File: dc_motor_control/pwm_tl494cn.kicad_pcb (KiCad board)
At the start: 2 copper layers, 70.6 x 45.5 mm, 46 parts, among them J1 PWR, J2 12V_SEL: up=src dn=reg, J3 MOT, Q1 RFP70N06, Q2 RFP70N06, Q3 RFP70N06, Q4 RFP70N06, Q5 BD139, Q6 BD140, U1 LM317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

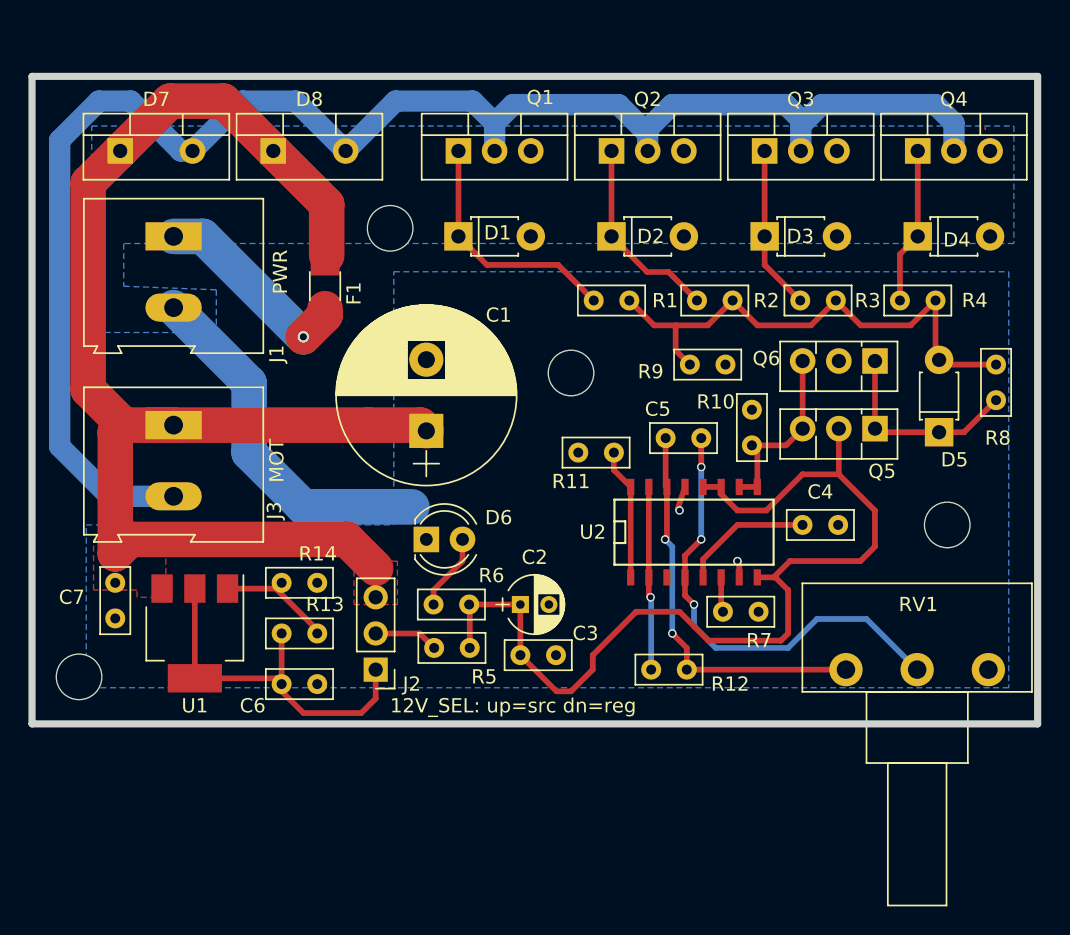
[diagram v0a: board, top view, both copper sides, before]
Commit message: Refining the DC motor control some more
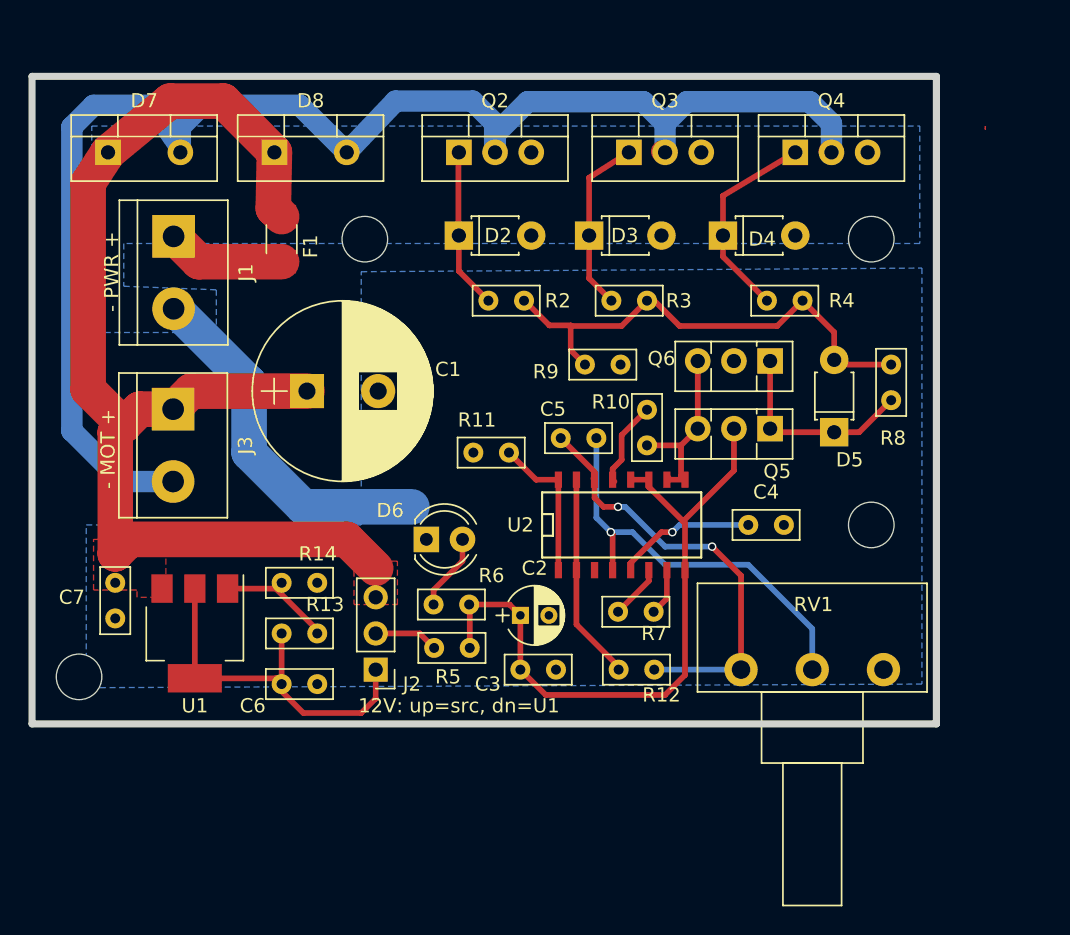
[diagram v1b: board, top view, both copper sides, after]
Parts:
- removed D1: 15V, Diodes_ThroughHole:D_T-1_P5.08mm_Horizontal
- removed Q1: RFP70N06, TO_SOT_Packages_THT:TO-220-3_Vertical
- removed R1: 10R, Capacitors_ThroughHole:C_Rect_L4.6mm_W2.0mm_P2.50mm_MKS02_FKP02
- J1: value PWR -> - PWR +; footprint Terminal_Blocks:TerminalBlock_Altech_AK300-2_P5.00mm -> Terminal_Blocks:TerminalBlock_bornier-2_P5.08mm
- J2: value 12V_SEL: up=src dn=reg -> 12V: up=src, dn=U1
- J3: value MOT -> - MOT +; footprint Terminal_Blocks:TerminalBlock_Altech_AK300-2_P5.00mm -> Terminal_Blocks:TerminalBlock_bornier-2_P5.08mm
- moved REF** 23.1 mm to (189.7, 91.7)
- moved R2 14.6 mm to (165.4, 96.0)
- moved D4 13.7 mm to (179.3, 91.4)
- moved R3 13.3 mm to (174.0, 96.0)
- moved D3 12.3 mm to (169.9, 91.4)
- moved Q2 10.7 mm to (160.8, 85.6)
- moved D2 10.7 mm to (160.8, 91.4)
- moved Q3 9.53 mm to (172.7, 85.6)
- moved R4 9.34 mm to (184.9, 96.0)
- moved C1 8.84 mm to (150.1, 102.4), turned to 0 degrees
- moved Q4 8.60 mm to (184.4, 85.6)
- moved C5 7.37 mm to (170.4, 105.7)
- moved D5 7.37 mm to (187.1, 105.2)
- moved Q5 7.37 mm to (182.6, 105.0)
- moved Q6 7.37 mm to (182.6, 100.2)
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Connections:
- U2 pad 3: Net-(U2-Pad3) -> (no net)
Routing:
- net +12V: track 68.4 -> 47.7 mm
- net Net-(D1-Pad1): track 17.4 -> 0.00 mm
- net Net-(C1-Pad1): track 95.8 -> 82.6 mm
- net Net-(D7-Pad2): track 112.9 -> 102.0 mm
- net GND: track 28.4 -> 34.8 mm, vias 2 -> 0
- net Net-(F1-Pad1): track 14.6 -> 8.32 mm, vias 1 -> 0
- net Net-(D4-Pad1): track 11.0 -> 14.6 mm
- net Net-(C5-Pad1): track 32.6 -> 29.6 mm, vias 3 -> 1
- net Net-(D2-Pad1): track 13.9 -> 11.4 mm
- net Net-(C5-Pad2): track 28.2 -> 30.5 mm
- net Net-(D5-Pad2): track 37.4 -> 35.2 mm
- net Net-(R12-Pad2): track 13.1 -> 14.8 mm, vias 1 -> 0
- net Net-(R7-Pad1): track 2.47 -> 3.99 mm
- net Net-(R11-Pad2): track 9.25 -> 10.6 mm
- net Net-(D3-Pad1): track 11.5 -> 12.7 mm
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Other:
- board size 70.6 x 45.5 mm -> 63.5 x 45.5 mm

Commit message: some more minor changes to the DC motor control PCB
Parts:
- moved R9 2.76 mm to (166.9, 100.6), turned to 180 degrees
- moved C5 1.02 mm to (170.4, 104.6)
- moved R10 1.02 mm to (174.0, 105.2)
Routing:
- net Net-(C5-Pad1): track 29.6 -> 30.6 mm
- net GND: track 34.8 -> 35.8 mm
- net Net-(C5-Pad2): track 30.5 -> 31.3 mm
- net Net-(Q5-Pad3): track 12.8 -> 13.3 mm
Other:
- board text added: "github.com/jonronen/kicad-stuff"
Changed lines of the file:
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@@
     (area 124.254857 80.013999 199.595143 139.195001)
     (thickness 1.6)
-    (drawings 4)
-    (tracks 172)
+    (drawings 5)
+    (tracks 175)
     (zones 0)
     (modules 43)
@@
     (last_trace_width 0.4)
     (trace_clearance 0.2)
-    (zone_clearance 1)
+    (zone_clearance 0.7)
     (zone_45_only no)
     (trace_min 0.2)
@@
   )
   (module Capacitors_ThroughHole:C_Rect_L4.6mm_W2.0mm_P2.50mm_MKS02_FKP02 (layer F.Cu)
-    (at 173.99 106.172 90)
+    (at 173.99 105.156 90)
     (descr "C, Rect series, Radial, pin pitch=2.50mm, , length*width=4.6*2mm^2, Capacitor, http://www.wima.de/DE/WIMA_MKS_02.pdf")
     (tags "C Rect series Radial pin pitch 2.50mm  length 4.6mm width 2mm Capacitor")
-    (fp_text reference R10 (at 3.048 -2.54 180) (layer F.SilkS)
+    (fp_text reference R10 (at 4.572 -2.54 180) (layer F.SilkS)
       (effects (font (size 1 1) (thickness 0.15)))
     )
@@
   )
   (module Capacitors_ThroughHole:C_Rect_L4.6mm_W2.0mm_P2.50mm_MKS02_FKP02 (layer F.Cu)
-    (at 170.434 105.664 180)
+    (at 170.434 104.648 180)
     (descr "C, Rect series, Radial, pin pitch=2.50mm, , length*width=4.6*2mm^2, Capacitor, http://www.wima.de/DE/WIMA_MKS_02.pdf")
     (tags "C Rect series Radial pin pitch 2.50mm  length 4.6mm width 2mm Capacitor")
-    (fp_text reference C5 (at 3.048 2.032 180) (layer F.SilkS)
+    (fp_text reference C5 (at 1.016 2.032 180) (layer F.SilkS)
       (effects (font (size 1 1) (thickness 0.15)))
     )
@@
   )
   (module Capacitors_ThroughHole:C_Rect_L4.6mm_W2.0mm_P2.50mm_MKS02_FKP02 (layer F.Cu)
-    (at 169.634 100.5)
+    (at 166.878 100.584 180)
     (descr "C, Rect series, Radial, pin pitch=2.50mm, , length*width=4.6*2mm^2, Capacitor, http://www.wima.de/DE/WIMA_MKS_02.pdf")
     (tags "C Rect series Radial pin pitch 2.50mm  length 4.6mm width 2mm Capacitor")
-    (fp_text reference R9 (at -2.75 0.5) (layer F.SilkS)
-      (effects (font (size 1 1) (thickness 0.15)))
-    )
-    (fp_text value 10K (at 1.25 2.31) (layer F.Fab) hide
+    (fp_text reference R9 (at 2.54 -2.032 180) (layer F.SilkS)
+      (effects (font (size 1 1) (thickness 0.15)))
+    )
+    (fp_text value 10K (at 1.25 2.31 180) (layer F.Fab) hide
       (effects (font (size 1 1) (thickness 0.15)))
     )
@@
     (fp_line (start 3.9 1.35) (end 3.9 -1.35) (layer F.CrtYd) (width 0.05))
     (fp_line (start 3.9 -1.35) (end -1.4 -1.35) (layer F.CrtYd) (width 0.05))
-    (fp_text user %R (at 1.25 0) (layer F.Fab) hide
-      (effects (font (size 1 1) (thickness 0.15)))
-    )
-    (pad 1 thru_hole circle (at 0 0) (size 1.4 1.4) (drill 0.7) (layers *.Cu *.Mask)
+    (fp_text user %R (at 1.25 0 180) (layer F.Fab) hide
+      (effects (font (size 1 1) (thickness 0.15)))
+    )
+    (pad 1 thru_hole circle (at 0 0 180) (size 1.4 1.4) (drill 0.7) (layers *.Cu *.Mask)
       (net 10 "Net-(D5-Pad2)"))
-    (pad 2 thru_hole circle (at 2.5 0) (size 1.4 1.4) (drill 0.7) (layers *.Cu *.Mask)
+    (pad 2 thru_hole circle (at 2.5 0 180) (size 1.4 1.4) (drill 0.7) (layers *.Cu *.Mask)
       (net 2 GND))
     (model ${KISYS3DMOD}/Capacitors_THT.3dshapes/C_Rect_L4.6mm_W2.0mm_P2.50mm_MKS02_FKP02.wrl
@@
     (descr "C, Rect series, Radial, pin pitch=2.50mm, , length*width=4.6*2mm^2, Capacitor, http://www.wima.de/DE/WIMA_MKS_02.pdf")
     (tags "C Rect series Radial pin pitch 2.50mm  length 4.6mm width 2mm Capacitor")
-    (fp_text reference R11 (at 0.254 -2.286) (layer F.SilkS)
+    (fp_text reference R11 (at 0 -2.032) (layer F.SilkS)
       (effects (font (size 1 1) (thickness 0.15)))
     )
@@
     )
   )
+  (gr_text github.com/jonronen/kicad-stuff (at 132.334 100.076 90) (layer F.SilkS)
+    (effects (font (size 1.5 1.5) (thickness 0.3)))
+  )
   (gr_line (start 130.81 80.264) (end 194.31 80.264) (angle 90) (layer Edge.Cuts) (width 0.5))
   (gr_line (start 130.81 125.73) (end 130.81 80.264) (angle 90) (layer Edge.Cuts) (width 0.5))
@@
   (segment (start 144.25 82) (end 147.828 85.598) (width 2.5) (layer F.Cu) (net 1) (status 20))
   (segment (start 140.5 82) (end 144.25 82) (width 2.5) (layer F.Cu) (net 1))
-  (segment (start 173.99 103.672) (end 172.212 105.45) (width 0.4) (layer F.Cu) (net 2))
-  (segment (start 171.577 107.823) (end 171.577 108.585) (width 0.4) (layer F.Cu) (net 2))
-  (segment (start 172.212 107.188) (end 171.577 107.823) (width 0.4) (layer F.Cu) (net 2))
-  (segment (start 172.212 105.45) (end 172.212 107.188) (width 0.4) (layer F.Cu) (net 2))
+  (segment (start 173.99 102.656) (end 172.252 104.394) (width 0.4) (layer F.Cu) (net 2))
+  (segment (start 171.577 107.061) (end 171.577 108.585) (width 0.4) (layer F.Cu) (net 2))
+  (segment (start 172.252 106.386) (end 171.577 107.061) (width 0.4) (layer F.Cu) (net 2))
+  (segment (start 172.252 104.394) (end 172.252 106.386) (width 0.4) (layer F.Cu) (net 2))
   (segment (start 174.458 117.856) (end 175.387 116.927) (width 0.4) (layer F.Cu) (net 2))
   (segment (start 175.387 116.927) (end 175.387 114.935) (width 0.4) (layer F.Cu) (net 2))
@@
   (segment (start 175.26 114.554) (end 181.102 114.554) (width 0.4) (layer B.Cu) (net 4))
   (segment (start 172.974 112.268) (end 175.26 114.554) (width 0.4) (layer B.Cu) (net 4))
-  (segment (start 170.434 105.664) (end 170.434 111.252) (width 0.4) (layer B.Cu) (net 4))
+  (segment (start 170.434 104.648) (end 170.434 111.252) (width 0.4) (layer B.Cu) (net 4) (status 10))
   (segment (start 171.577 112.395) (end 171.577 114.935) (width 0.4) (layer F.Cu) (net 4))
   (segment (start 171.45 112.268) (end 171.577 112.395) (width 0.4) (layer F.Cu) (net 4))
@@
   (segment (start 180.594 115.316) (end 178.562 113.284) (width 0.4) (layer F.Cu) (net 5))
   (segment (start 174.498 121.92) (end 180.594 121.92) (width 0.4) (layer B.Cu) (net 5))
-  (segment (start 167.934 105.664) (end 170.307 108.037) (width 0.4) (layer F.Cu) (net 5))
+  (segment (start 167.934 104.648) (end 170.307 108.037) (width 0.4) (layer F.Cu) (net 5) (status 10))
   (segment (start 170.307 108.037) (end 170.307 108.585) (width 0.4) (layer F.Cu) (net 5))
   (segment (start 170.22 108.498) (end 170.307 108.585) (width 0.4) (layer F.Cu) (net 5) (status 30))
@@
   (segment (start 182.884 105.25) (end 187.134 105.25) (width 0.4) (layer F.Cu) (net 9))
   (segment (start 182.634 100.25) (end 182.634 105) (width 0.4) (layer F.Cu) (net 9))
+  (segment (start 166.878 100.584) (end 168.402 99.06) (width 0.4) (layer F.Cu) (net 10))
+  (segment (start 168.402 99.06) (end 168.402 97.75) (width 0.4) (layer F.Cu) (net 10))
   (segment (start 184.912 96.012) (end 187.134 98.234) (width 0.4) (layer F.Cu) (net 10))
   (segment (start 187.134 98.234) (end 187.134 100.17) (width 0.4) (layer F.Cu) (net 10))
@@
   (segment (start 168.634 97.79) (end 172.212 97.79) (width 0.4) (layer F.Cu) (net 10))
   (segment (start 172.212 97.79) (end 173.99 96.012) (width 0.4) (layer F.Cu) (net 10))
-  (segment (start 169.634 100.5) (end 168.634 99.5) (width 0.4) (layer F.Cu) (net 10))
-  (segment (start 168.634 99.5) (end 168.634 97.79) (width 0.4) (layer F.Cu) (net 10))
   (segment (start 168.634 97.79) (end 168.634 97.75) (width 0.4) (layer F.Cu) (net 10))
   (segment (start 167.134 97.75) (end 165.384 96) (width 0.4) (layer F.Cu) (net 10))
-  (segment (start 168.634 97.75) (end 167.134 97.75) (width 0.4) (layer F.Cu) (net 10))
+  (segment (start 168.634 97.75) (end 168.402 97.75) (width 0.4) (layer F.Cu) (net 10))
+  (segment (start 168.402 97.75) (end 167.134 97.75) (width 0.4) (layer F.Cu) (net 10))
   (segment (start 186.884 99.92) (end 187.464 100.5) (width 0.4) (layer F.Cu) (net 10))
   (segment (start 187.464 100.5) (end 191.134 100.5) (width 0.4) (layer F.Cu) (net 10))
@@
   (segment (start 161.544 120.396) (end 161.544 117.388) (width 0.4) (layer F.Cu) (net 14))
   (segment (start 161.544 117.388) (end 161.584 117.348) (width 0.4) (layer F.Cu) (net 14))
-  (segment (start 176.382 106.172) (end 176.382 108.31) (width 0.4) (layer F.Cu) (net 15))
+  (segment (start 173.99 105.156) (end 175.006 105.156) (width 0.4) (layer F.Cu) (net 15))
+  (segment (start 175.006 105.156) (end 176.382 106.532) (width 0.4) (layer F.Cu) (net 15))
+  (segment (start 176.382 106.172) (end 176.382 106.532) (width 0.4) (layer F.Cu) (net 15))
+  (segment (start 176.382 106.532) (end 176.382 108.31) (width 0.4) (layer F.Cu) (net 15))
   (segment (start 176.382 108.31) (end 176.657 108.585) (width 0.4) (layer F.Cu) (net 15))
   (segment (start 175.387 108.585) (end 175.514 108.458) (width 0.4) (layer F.Cu) (net 15))
-  (segment (start 173.99 106.172) (end 176.382 106.172) (width 0.4) (layer F.Cu) (net 15))
   (segment (start 176.382 106.172) (end 177.554 105) (width 0.4) (layer F.Cu) (net 15))
   (segment (start 175.387 108.585) (end 176.657 108.585) (width 0.4) (layer F.Cu) (net 15) (status 30))
@@
   )
   (zone (net 2) (net_name GND) (layer B.Cu) (hatch edge 0.508)
-    (connect_pads yes (clearance 1))
+    (connect_pads yes (clearance 0.7))
     (min_thickness 0.254)
     (fill yes (arc_segments 16) (thermal_gap 1) (thermal_bridge_width 0.508))
